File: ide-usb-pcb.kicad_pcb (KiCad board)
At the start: 2 copper layers, 31 parts, among them J1 Conn_02x20_Odd_Even, J2 STM32F4_Discovery_Header, J3 Screw_Terminal_01x02, J4 USB_B, U1 TXS0108EPW, U2 TXS0108EPW

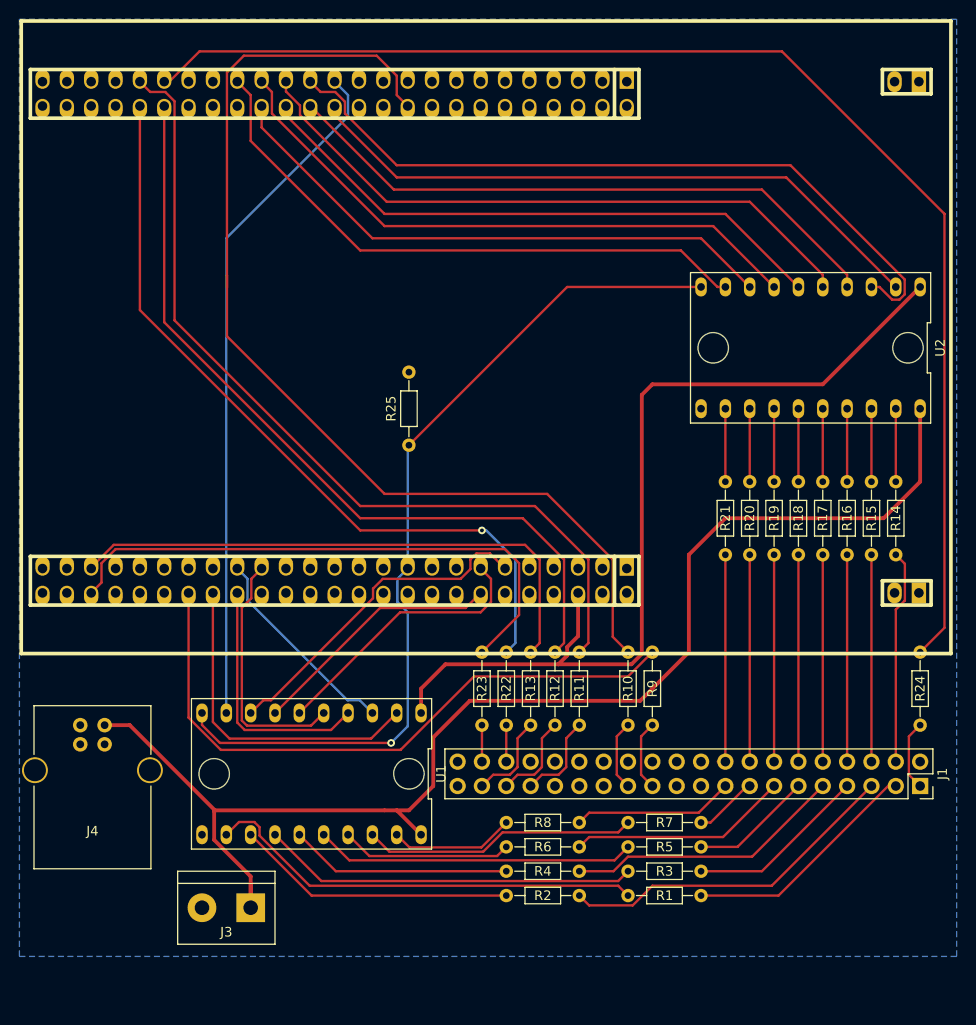
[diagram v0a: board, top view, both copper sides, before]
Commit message: Improve spacing between some traces
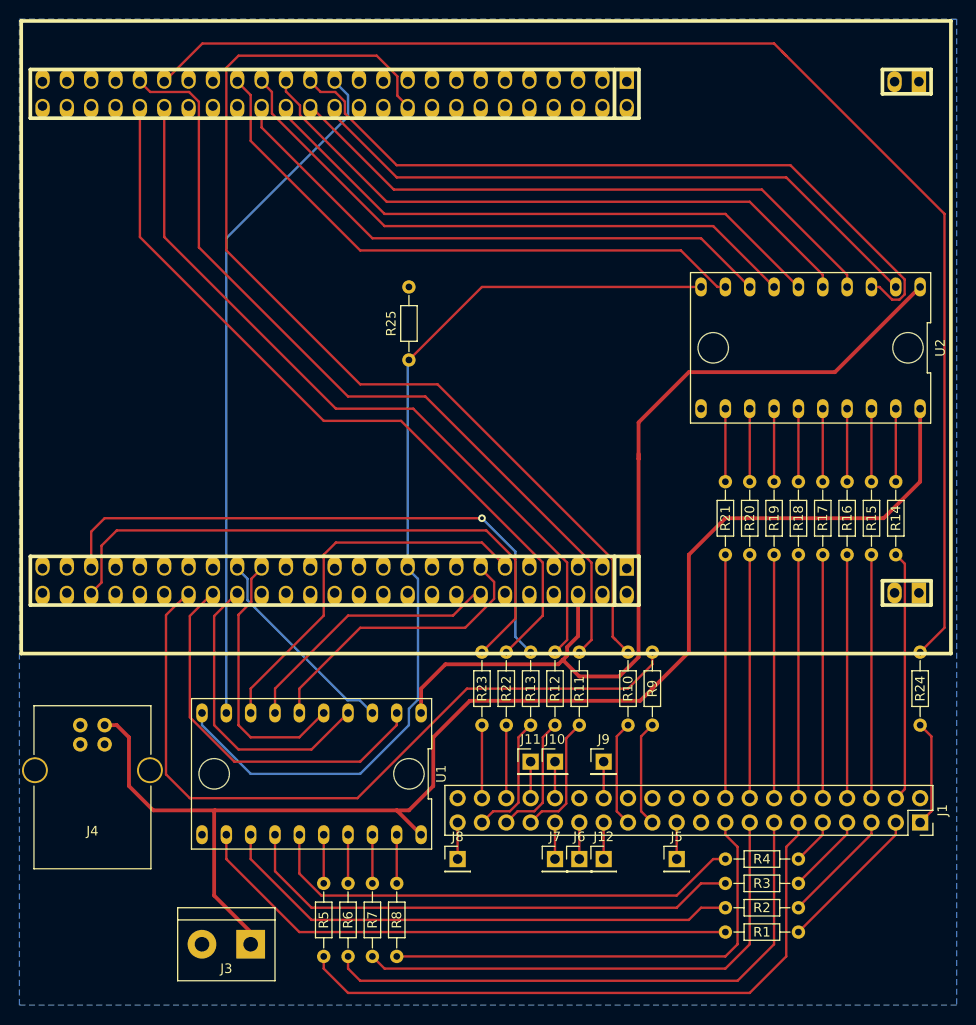
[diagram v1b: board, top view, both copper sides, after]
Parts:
- added J10: Conn_01x01_Male, Socket_Strips:Socket_Strip_Straight_1x01_Pitch2.54mm, F.Cu at (88.9, 120.7)
- added J11: Conn_01x01_Male, Socket_Strips:Socket_Strip_Straight_1x01_Pitch2.54mm, F.Cu at (86.4, 120.7)
- added J12: Conn_01x01_Male, Socket_Strips:Socket_Strip_Straight_1x01_Pitch2.54mm, F.Cu at (94.0, 130.8)
- added J5: Conn_01x01_Male, Socket_Strips:Socket_Strip_Straight_1x01_Pitch2.54mm, F.Cu at (101.6, 130.8)
- added J6: Conn_01x01_Male, Socket_Strips:Socket_Strip_Straight_1x01_Pitch2.54mm, F.Cu at (91.4, 130.8)
- added J7: Conn_01x01_Male, Socket_Strips:Socket_Strip_Straight_1x01_Pitch2.54mm, F.Cu at (88.9, 130.8)
- added J8: Conn_01x01_Male, Socket_Strips:Socket_Strip_Straight_1x01_Pitch2.54mm, F.Cu at (78.7, 130.8)
- added J9: Conn_01x01_Male, Socket_Strips:Socket_Strip_Straight_1x01_Pitch2.54mm, F.Cu at (94.0, 120.7)
- moved R5 41.0 mm to (64.8, 141.0), turned to 90 degrees
- moved R7 37.0 mm to (69.8, 141.0), turned to 90 degrees
- moved R6 26.7 mm to (67.3, 141.0), turned to 90 degrees
- moved R8 23.6 mm to (72.4, 141.0), turned to 90 degrees
- moved R2 22.9 mm to (114.3, 135.9)
- moved R4 22.9 mm to (114.3, 130.8)
- moved R1 10.9 mm to (114.3, 138.4)
- moved R3 10.2 mm to (114.3, 133.3)
- moved R25 8.89 mm to (73.7, 78.7)
- moved J1 3.81 mm to (127.0, 127.0)
- moved J3 3.81 mm to (57.1, 139.7)
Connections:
- J1 pad 21: (no net) -> /DMARQ
- J1 pad 27: (no net) -> /IORDY
- J1 pad 28: (no net) -> /CSEL
- J1 pad 29: (no net) -> /DMACK
- J1 pad 31: (no net) -> /INTRQ
- J1 pad 32: (no net) -> /IOCS16
- J1 pad 34: (no net) -> /PDIAG
- J1 pad 39: (no net) -> /ACT
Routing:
- net Net-(J1-Pad11): track 12.8 -> 66.7 mm
- net Net-(J1-Pad15): track 6.66 -> 53.6 mm
- net Net-(J1-Pad13): track 23.0 -> 60.5 mm
- net Net-(J1-Pad17): track 16.8 -> 49.3 mm
- net /DD3B: track 33.4 -> 5.08 mm
- net /DD4B: track 23.2 -> 51.0 mm
- net /DD6B: track 29.3 -> 55.2 mm
- net Net-(J1-Pad9): track 29.1 -> 4.86 mm
- net Net-(J1-Pad5): track 36.1 -> 12.0 mm
- net /DD1B: track 28.7 -> 5.08 mm
- net /DD5B: track 39.3 -> 53.4 mm
- net /DD2B: track 17.8 -> 5.08 mm
- net /DIOW: track 67.0 -> 78.8 mm
- net /DD7B: track 46.2 -> 57.8 mm
- net Net-(J1-Pad7): track 18.9 -> 8.45 mm
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
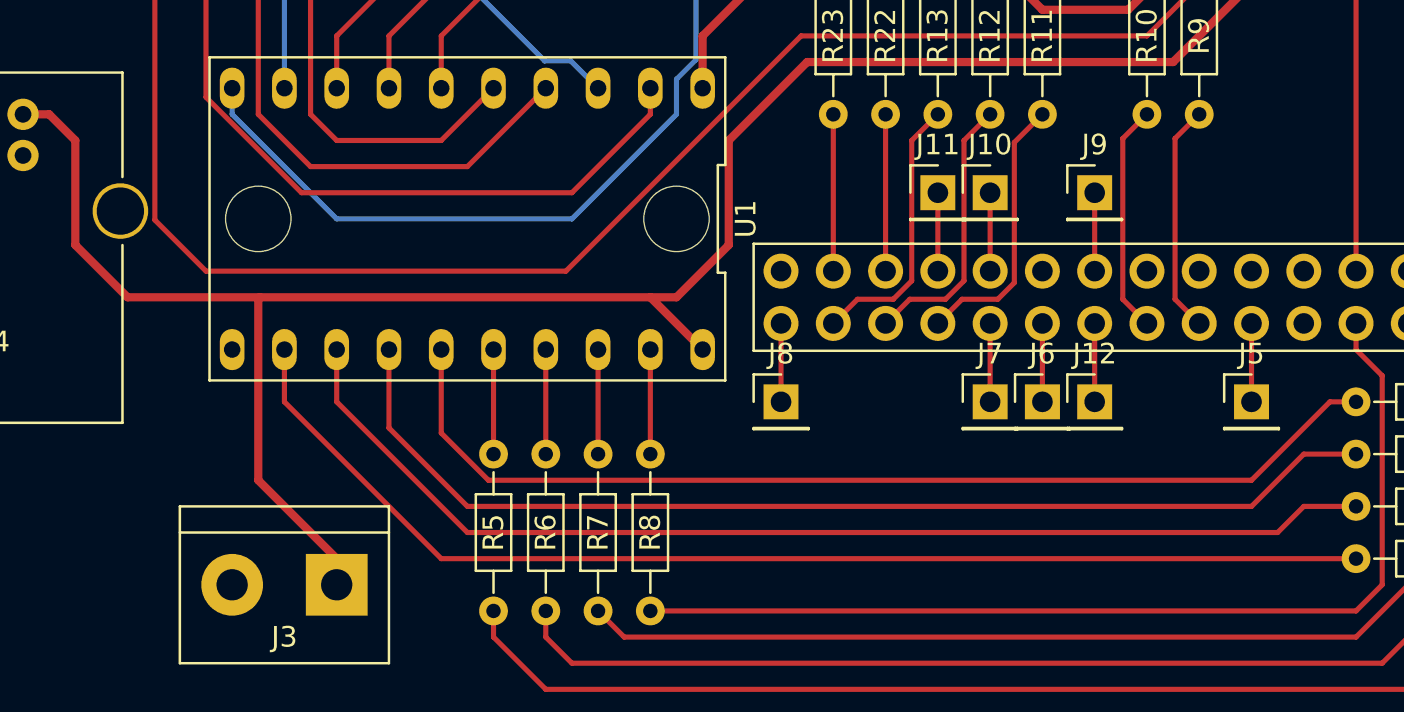
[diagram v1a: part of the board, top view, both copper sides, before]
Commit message: Add connectors for unused IDE signals
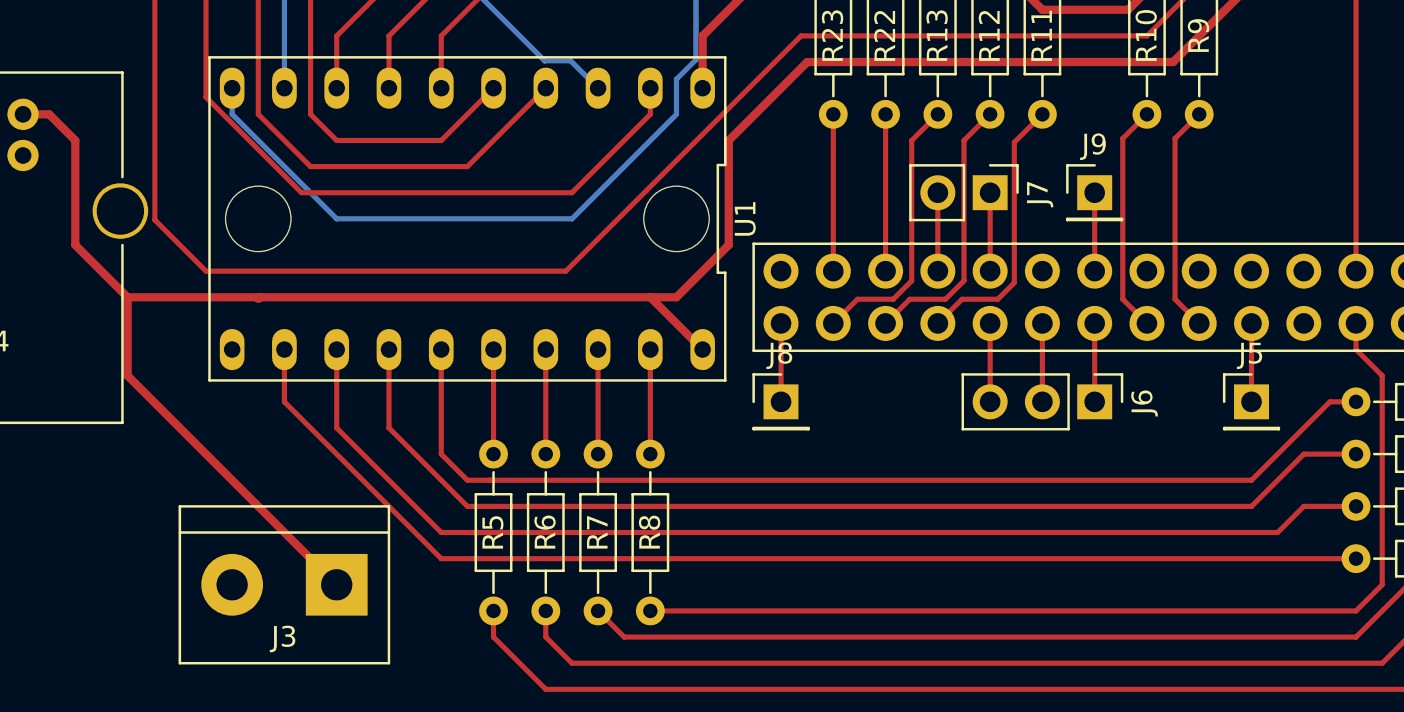
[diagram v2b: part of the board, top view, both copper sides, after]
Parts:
- removed J10, J11, J12: Conn_01x01_Male, Socket_Strips:Socket_Strip_Straight_1x01_Pitch2.54mm
- J6: value Conn_01x01_Male -> Conn_01x03_Male; footprint Socket_Strips:Socket_Strip_Straight_1x01_Pitch2.54mm -> Socket_Strips:Socket_Strip_Straight_1x03_Pitch2.54mm
- J7: value Conn_01x01_Male -> Conn_01x02_Male; footprint Socket_Strips:Socket_Strip_Straight_1x01_Pitch2.54mm -> Socket_Strips:Socket_Strip_Straight_1x02_Pitch2.54mm
- moved J7 10.2 mm to (88.9, 120.7), turned to 270 degrees
- moved J6 2.54 mm to (94.0, 130.8), turned to 270 degrees
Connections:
- J6 pad 1: /DMACK -> /IORDY
- J7 pad 1: /INTRQ -> /IOCS16
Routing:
- net +5V: track 141.7 -> 145.7 mm
- net /DD6B: track 55.2 -> 57.2 mm
- net /DD4B: track 51.0 -> 51.9 mm

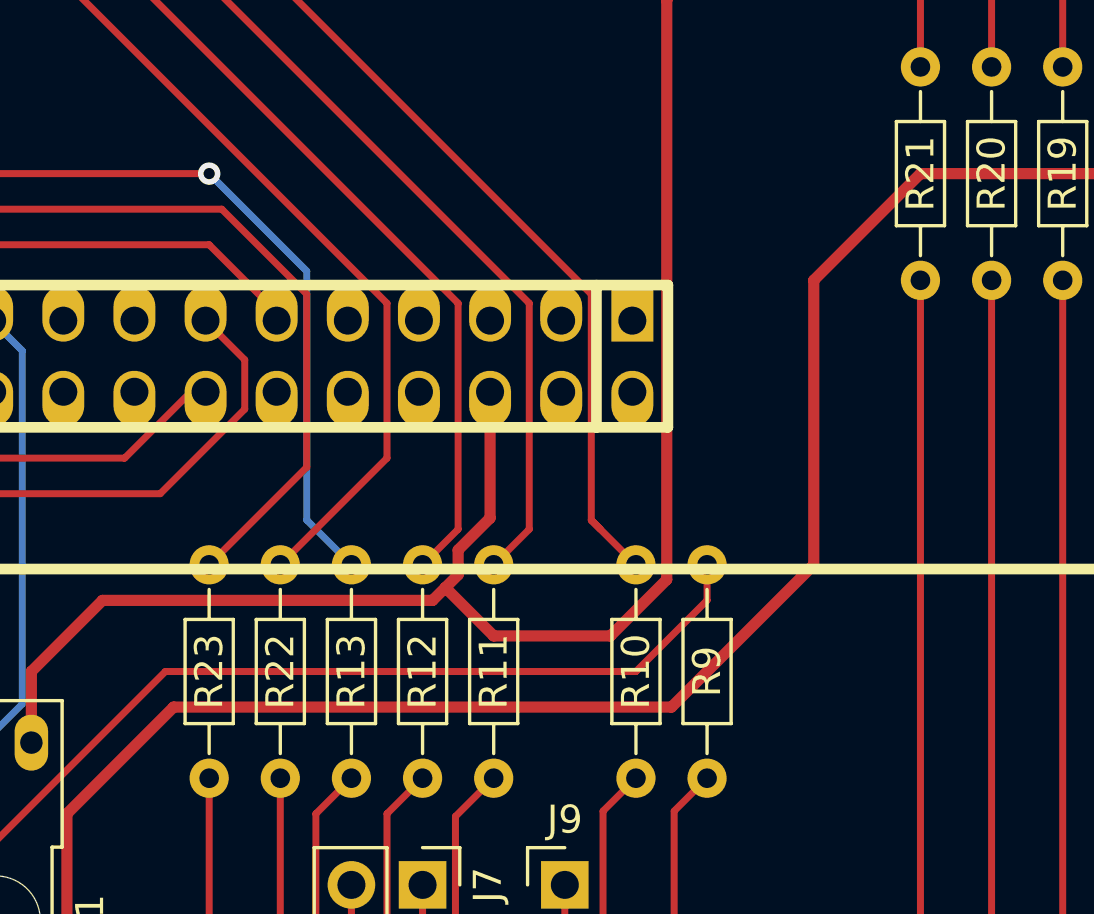
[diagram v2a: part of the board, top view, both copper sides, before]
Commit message: Add jumper to power STM discovery board
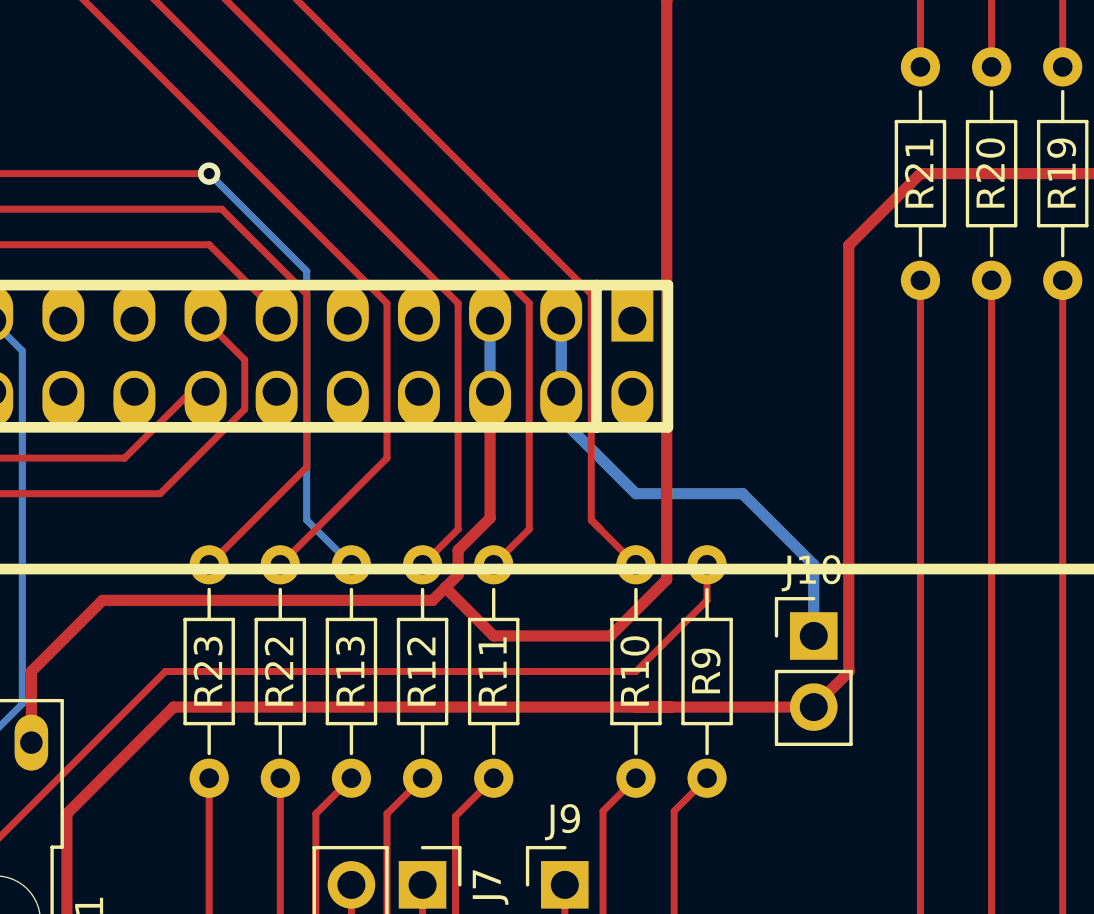
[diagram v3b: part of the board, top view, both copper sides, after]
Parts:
- added J10: Conn_01x02_Male, Socket_Strips:Socket_Strip_Straight_1x02_Pitch2.54mm, F.Cu at (102.9, 111.8)
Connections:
- J2 pad 95: (no net) -> +3V3
- J2 pad 97: (no net) -> /+5VBOARD
- J2 pad 98: (no net) -> /+5VBOARD
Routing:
- net /+5VBOARD: track 0.00 -> 17.2 mm
- net +5V: track 145.7 -> 149.9 mm
- net +3V3: track 95.9 -> 98.5 mm

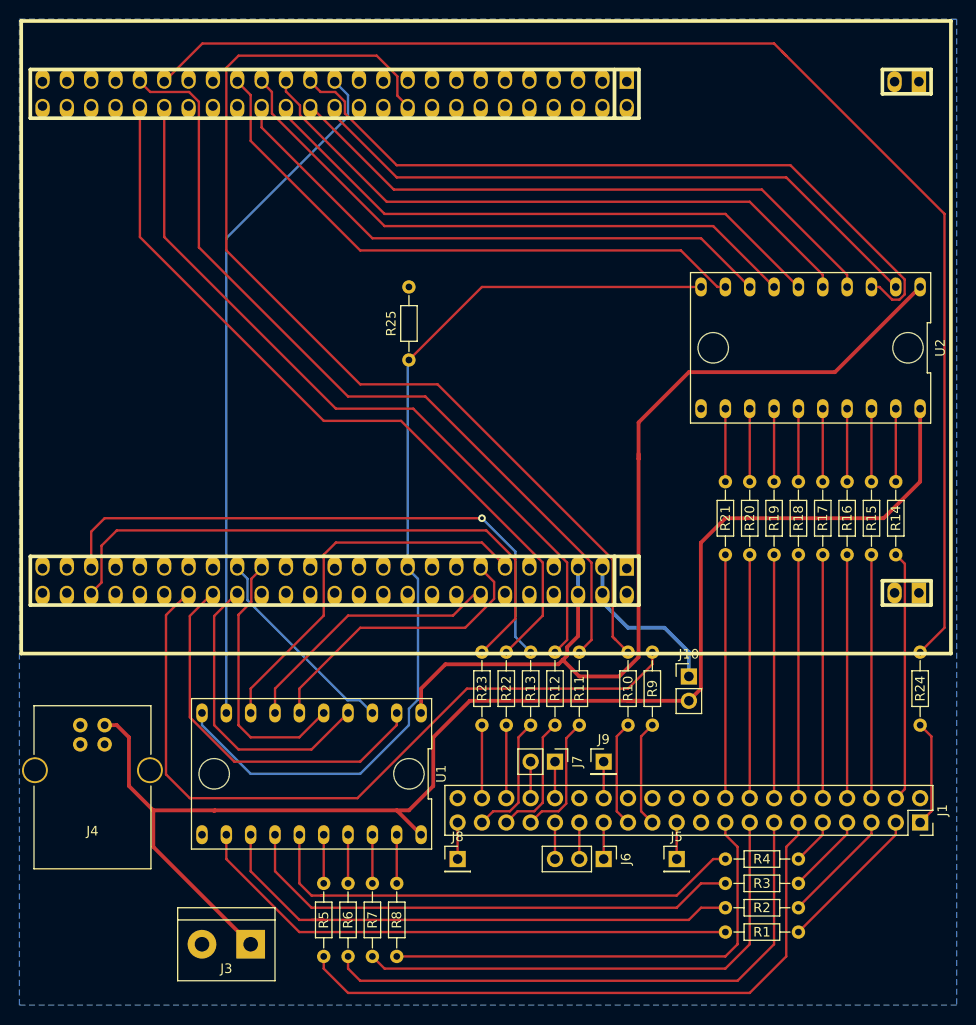
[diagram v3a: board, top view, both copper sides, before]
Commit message: Improve routing of some traces
Also improve placement of component names on silkscreen layer
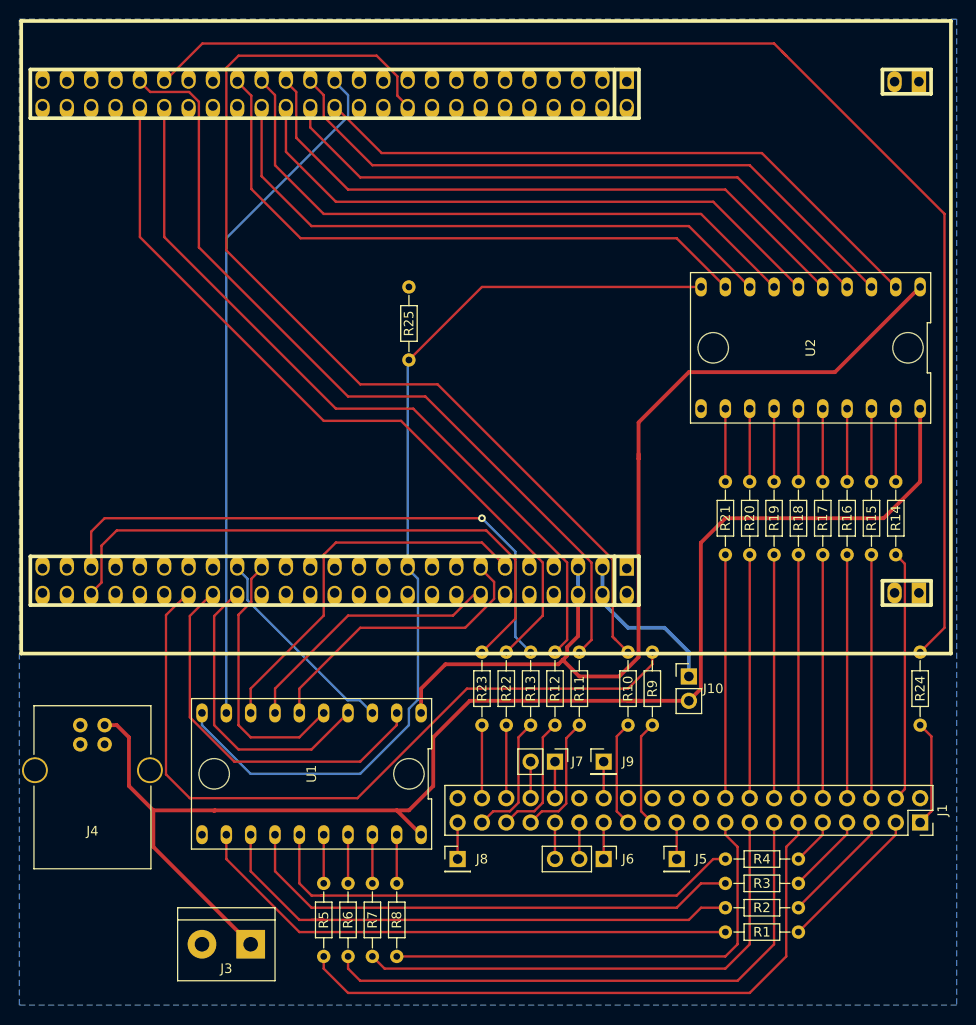
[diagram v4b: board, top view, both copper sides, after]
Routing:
- net /DD9A: track 77.1 -> 68.7 mm
- net /DD13A: track 63.7 -> 66.6 mm
- net /DD14A: track 60.1 -> 63.0 mm
- net /DD15A: track 62.6 -> 65.5 mm
- net /DD12A: track 61.9 -> 64.1 mm
- net /DD11A: track 66.8 -> 67.7 mm
- net /DD8A: track 66.9 -> 66.4 mm
- net /DD10A: track 64.6 -> 65.1 mm
